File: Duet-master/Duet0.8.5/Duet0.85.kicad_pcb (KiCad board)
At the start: 4 copper layers, 286.6 x 277.8 mm, 318 parts, among them J1 X VREF, J10 GND V_IN, J11 GND V_IN, J12 E1 TEMP, J13 Probe, J19 USB, J2 Z VREF, J20 uSDHC, J21 ETHERNET, J22 GND, J23 JTAG, J24 GND, J3 Y VREF, J4 E0 VREF, J5 E1 VREF, J6 EXPANSION, J7 PanelDUE, J8 POWER IN, J9 5V_PS, P1 CONN_4, P2 CONN_4, P3 CONN_4, P4 CONN_4, P5 CONN_4, P6 CONN_4, P7 CONN_4, P8 CONN_4, P9 CONN_4, U1 A4982SLPTR, U10 USB_3.0_Receptacle, U11 KSZ8051RNL, U12 ATSAM3X8E, U13 USB_3.0_Receptacle_4, U14 USB_3.0_Receptacle_4, U15 USB_3.0_Receptacle_4, U16 USB_3.0_Receptacle_4, U17 USB_3.0_Receptacle_4, U18 USB_3.0_Receptacle_3, U19 USB_3.0_Receptacle_2, U2 A4982SLPTR, U20 USB_3.0_Receptacle_2, U21 USB_3.0_Receptacle_3, U3 A4982SLPTR, U4 A4982SLPTR, U5 A4982SLPTR, U6 MCP44X1, U7 TC2117-3.3VDBTR, U8 A4403, U9 USB_3.0_Receptacle, X1 CRYSTAL_4PIN, X2 CRYSTAL_4PIN

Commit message: Nearly complete
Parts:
- removed the REF** at (111.9, 111.8)
- moved U7 95.7 mm to (254.9, 65.4)
- moved R26 10.7 mm to (171.2, 86.9), turned to 90 degrees
- moved J24 8.03 mm to (140.0, 97.3)
- moved R30 6.90 mm to (171.7, 90.5)
- moved C35 6.87 mm to (171.7, 93.7)
- moved R24 5.02 mm to (164.8, 77.8), turned to 0 degrees
- moved R21 4.71 mm to (164.8, 76.1), turned to 0 degrees
- moved C85 3.39 mm to (150.3, 69.8)
- moved D16 1.88 mm to (174.7, 71.5), turned to 270 degrees
- moved C86 1.59 mm to (150.3, 71.6)
- moved R54 1.17 mm to (94.4, 62.4), turned to 180 degrees
- moved J5 0.50 mm to (180.1, 80.0)
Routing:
- net GND: track 992.8 -> 1460.4 mm, vias 63 -> 90
- net Y_EN: track 6.94 -> 197.0 mm, vias 1 -> 6
- net Y_DIR: track 6.15 -> 175.7 mm, vias 1 -> 4
- net X_EN: track 7.30 -> 176.3 mm, vias 1 -> 6
- net Y_STEP: track 10.7 -> 167.5 mm, vias 1 -> 3
- net E0_EN: track 7.17 -> 161.1 mm, vias 1 -> 6
- net X_DIR: track 6.22 -> 154.5 mm, vias 1 -> 2
- net X_STEP: track 9.85 -> 146.4 mm, vias 1 -> 2
- net E0_DIR: track 6.04 -> 138.3 mm, vias 1 -> 2
- net E0_STEP: track 9.00 -> 130.8 mm, vias 1 -> 2
- net Z_EN: track 81.5 -> 179.4 mm, vias 4 -> 6
- net +3.3V: track 491.6 -> 586.2 mm, vias 23 -> 30
- net Z_DIR: track 80.2 -> 158.4 mm
- net Z_STEP: track 89.0 -> 150.1 mm
- net TWCK0: track 106.1 -> 52.6 mm, vias 6 -> 2
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
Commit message: Clean up
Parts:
- moved D16 9.56 mm to (180.0, 63.5)
- moved U7 4.06 mm to (250.9, 65.8), turned to 90 degrees
- moved R61 2.53 mm to (170.5, 70.3)
- moved JP2 2.11 mm to (116.1, 89.8), turned to 270 degrees
- moved C43 1.92 mm to (159.4, 76.8)
- moved C47 1.79 mm to (159.4, 78.6)
- moved D13 1.61 mm to (115.2, 84.0)
- moved D14 1.61 mm to (115.2, 86.1)
- moved C92 1.59 mm to (111.3, 78.5)
- moved L3 1.57 mm to (114.5, 78.5)
- moved C72 1.51 mm to (114.5, 80.2)
- moved C71 1.51 mm to (114.5, 82.0)
- moved C35 1.45 mm to (172.6, 94.9)
- moved C49 1.43 mm to (124.4, 94.0)
- moved C50 1.40 mm to (122.3, 94.0)
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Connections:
- net LED0_B_PWM renamed PC23_PWML6
- net LED1_B_PWM renamed PC18_PWMH6
- net LED1_G_PWM renamed PC20_PWMH4
- net PC21_PWML4 renamed LED0_G_PWM
- U10 pad 10: (no net) -> GND
- U13 pad 10: (no net) -> GND
- U14 pad 10: (no net) -> GND
- U15 pad 10: (no net) -> GND
- U16 pad 10: (no net) -> GND
- U17 pad 10: (no net) -> GND
- U18 pad 10: (no net) -> GND
- U19 pad 10: (no net) -> GND
- U20 pad 10: (no net) -> GND
- U21 pad 10: (no net) -> GND
- U9 pad 10: (no net) -> GND
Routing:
- net (no net): track 3409.6 -> 7.18 mm, vias 0 -> 167
- net +5V: track 46.3 -> 765.4 mm, vias 0 -> 17
- net GND: track 1460.4 -> 1984.3 mm, vias 90 -> 170
- net +3.3V: track 586.2 -> 956.4 mm, vias 30 -> 54
- net V_IN: track 838.2 -> 1070.2 mm, vias 19 -> 29
- net VSSA: track 334.8 -> 469.5 mm, vias 9 -> 16
- net Z_REF: track 3.70 -> 106.8 mm, vias 0 -> 4
- net Y_REF: track 5.37 -> 90.5 mm, vias 0 -> 2
- net E1_EN: track 23.2 -> 101.0 mm, vias 2 -> 3
- net E1_DIR: track 0.00 -> 72.8 mm, vias 0 -> 2
- net FAN0_PWM: track 1.71 -> 72.4 mm, vias 0 -> 2
- net TWD0: track 83.1 -> 153.8 mm, vias 2 -> 7
- net X_REF: track 5.27 -> 74.3 mm, vias 0 -> 2
- net /Processor/VDDCORE: track 56.8 -> 117.7 mm, vias 2 -> 6
- net TWCK0: track 52.6 -> 107.9 mm, vias 2 -> 8
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- added copper zone on B.Cu, net BED-
- added copper zone on B.Cu, net E0-
- added copper zone on B.Cu, net GND
- added copper zone on F.Cu, net GND

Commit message: Cleaned
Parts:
- H1: renamed from P9; value CONN_4 -> 4 PIN
- H2: renamed from P8; value CONN_4 -> 4 PIN
- H3: renamed from P7; value CONN_4 -> 4 PIN
- H4: renamed from P6; value CONN_4 -> 4 PIN
- H5: renamed from P5; value CONN_4 -> 4 PIN
- H6: renamed from P4; value CONN_4 -> 4 PIN
- H7: renamed from P3; value CONN_4 -> 4 PIN
- H8: renamed from P2; value CONN_4 -> 4 PIN
- H9: renamed from P1; value CONN_4 -> 4 PIN
- USB 1: renamed from U21; value USB_3.0_Receptacle_3 -> SENSE 2
- USB 10: renamed from U14; value USB_3.0_Receptacle_4 -> MOTOR 4
- USB 11: renamed from U13; value USB_3.0_Receptacle_4 -> MOTOR 5
- USB 2: renamed from U18; value USB_3.0_Receptacle_3 -> SENSE 1
- USB 3: renamed from U9; value USB_3.0_Receptacle -> PWR/SENSE 1
- USB 4: renamed from U10; value USB_3.0_Receptacle -> PWR/SENSE 2
- USB 5: renamed from U20; value USB_3.0_Receptacle_2 -> LIGHT 2
- USB 6: renamed from U19; value USB_3.0_Receptacle_2 -> LIGHT 1
- USB 7: renamed from U17; value USB_3.0_Receptacle_4 -> MOTOR 1
- USB 8: renamed from U16; value USB_3.0_Receptacle_4 -> MOTOR 2
- USB 9: renamed from U15; value USB_3.0_Receptacle_4 -> MOTOR 3
- moved JP2 0.56 mm to (116.7, 89.8)
- moved R68 0.49 mm to (168.0, 58.8)
- moved J5 0.06 mm to (180.3, 79.5)
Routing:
- net GND: track 1984.3 -> 2346.4 mm, vias 170 -> 117
- net +3.3V: track 956.4 -> 1113.9 mm, vias 54 -> 63
- net V_IN: track 1070.2 -> 1115.7 mm, vias 29 -> 38
- net (no net): track 7.18 -> 0.33 mm, vias 167 -> 0
- net +5V: track 765.4 -> 761.3 mm
- net Net-(J21-Pad3): track 142.0 -> 139.0 mm
- net Net-(J21-Pad2): track 139.4 -> 136.7 mm
- net ENET_MDIO: track 52.9 -> 50.3 mm
- net Z_EN: track 176.5 -> 179.0 mm, vias 4 -> 5
- net SPI0_MOSI: track 91.6 -> 94.0 mm
- net E0_REF: track 56.0 -> 57.8 mm
- net E1_STEP: track 72.1 -> 70.3 mm
- net ENET_TX_EN: track 26.7 -> 28.0 mm
- net RESET: track 209.6 -> 208.4 mm
- net BED_PWM: track 61.7 -> 60.5 mm
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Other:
- board size 286.6 x 277.8 mm -> 281.1 x 277.8 mm

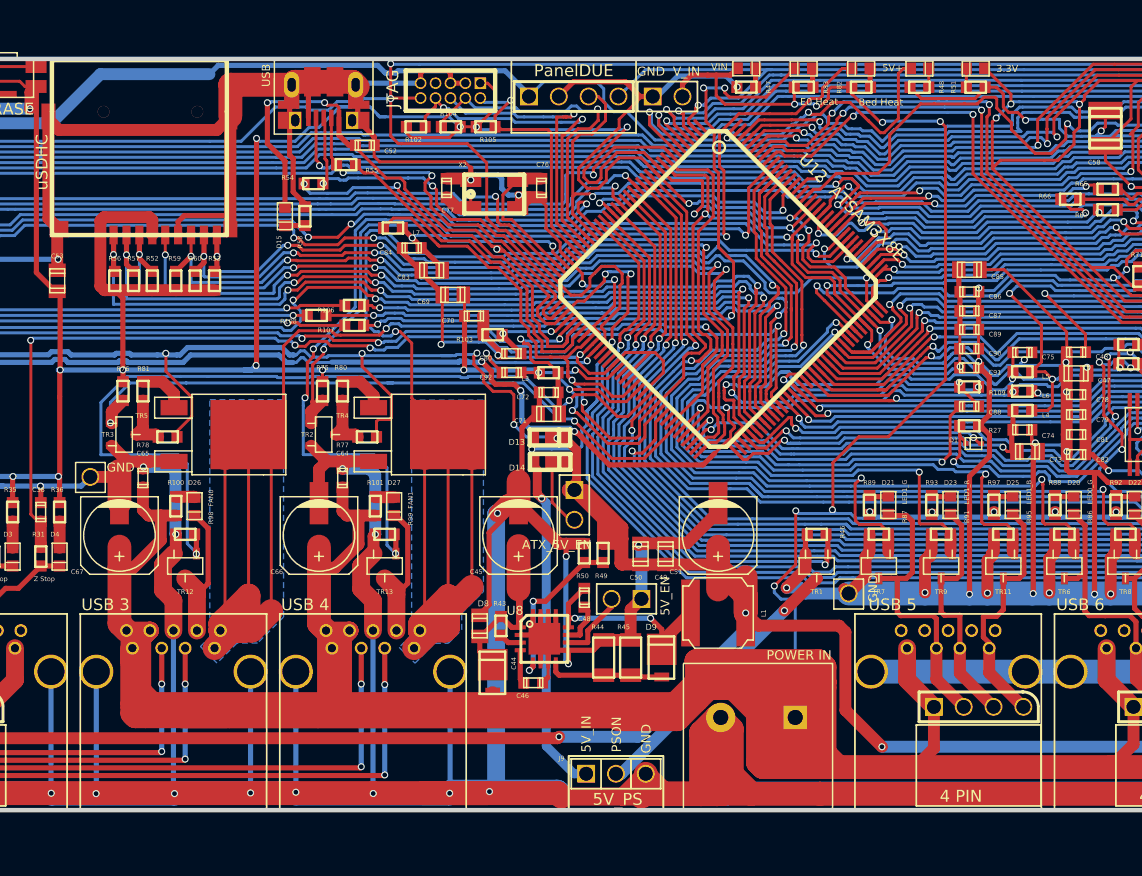
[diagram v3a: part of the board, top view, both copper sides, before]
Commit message: Some GND connections beefed up
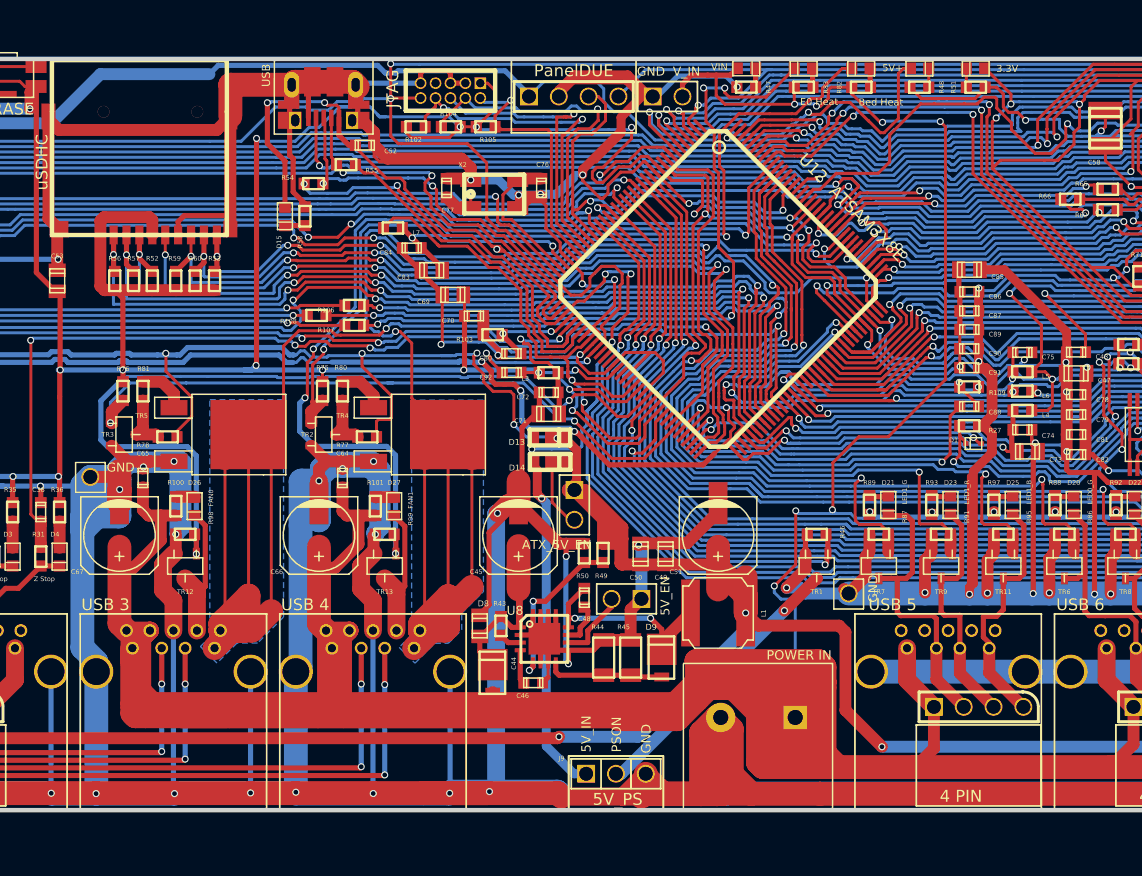
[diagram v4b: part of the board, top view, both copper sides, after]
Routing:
- net GND: track 2346.4 -> 2516.9 mm, vias 117 -> 124
- net +3.3V: track 1113.9 -> 1114.9 mm
- net PD9: track 94.9 -> 95.8 mm
- net URXD: track 107.5 -> 108.3 mm
